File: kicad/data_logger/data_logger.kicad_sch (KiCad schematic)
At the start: 20 parts, among them M2 Motor_DC, M3 Motor_DC, M4 Motor_Servo, SW1 SW_SPST, SW2 SW_Reed

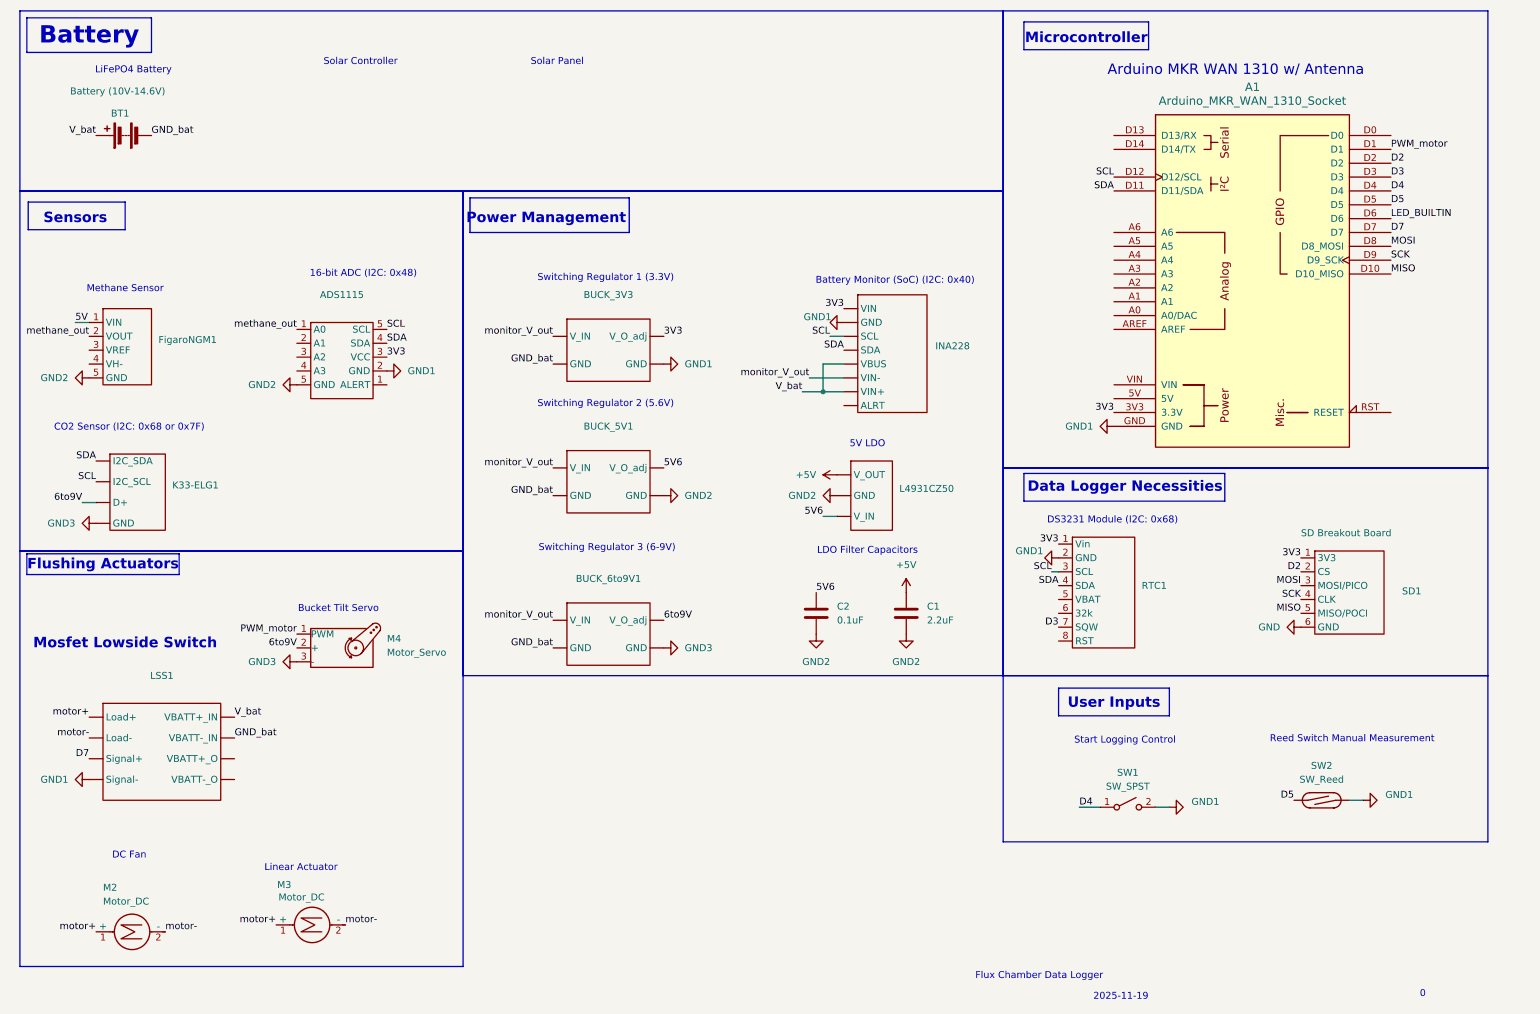
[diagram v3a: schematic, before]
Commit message: Schematic changes to add motor driver and routed traces
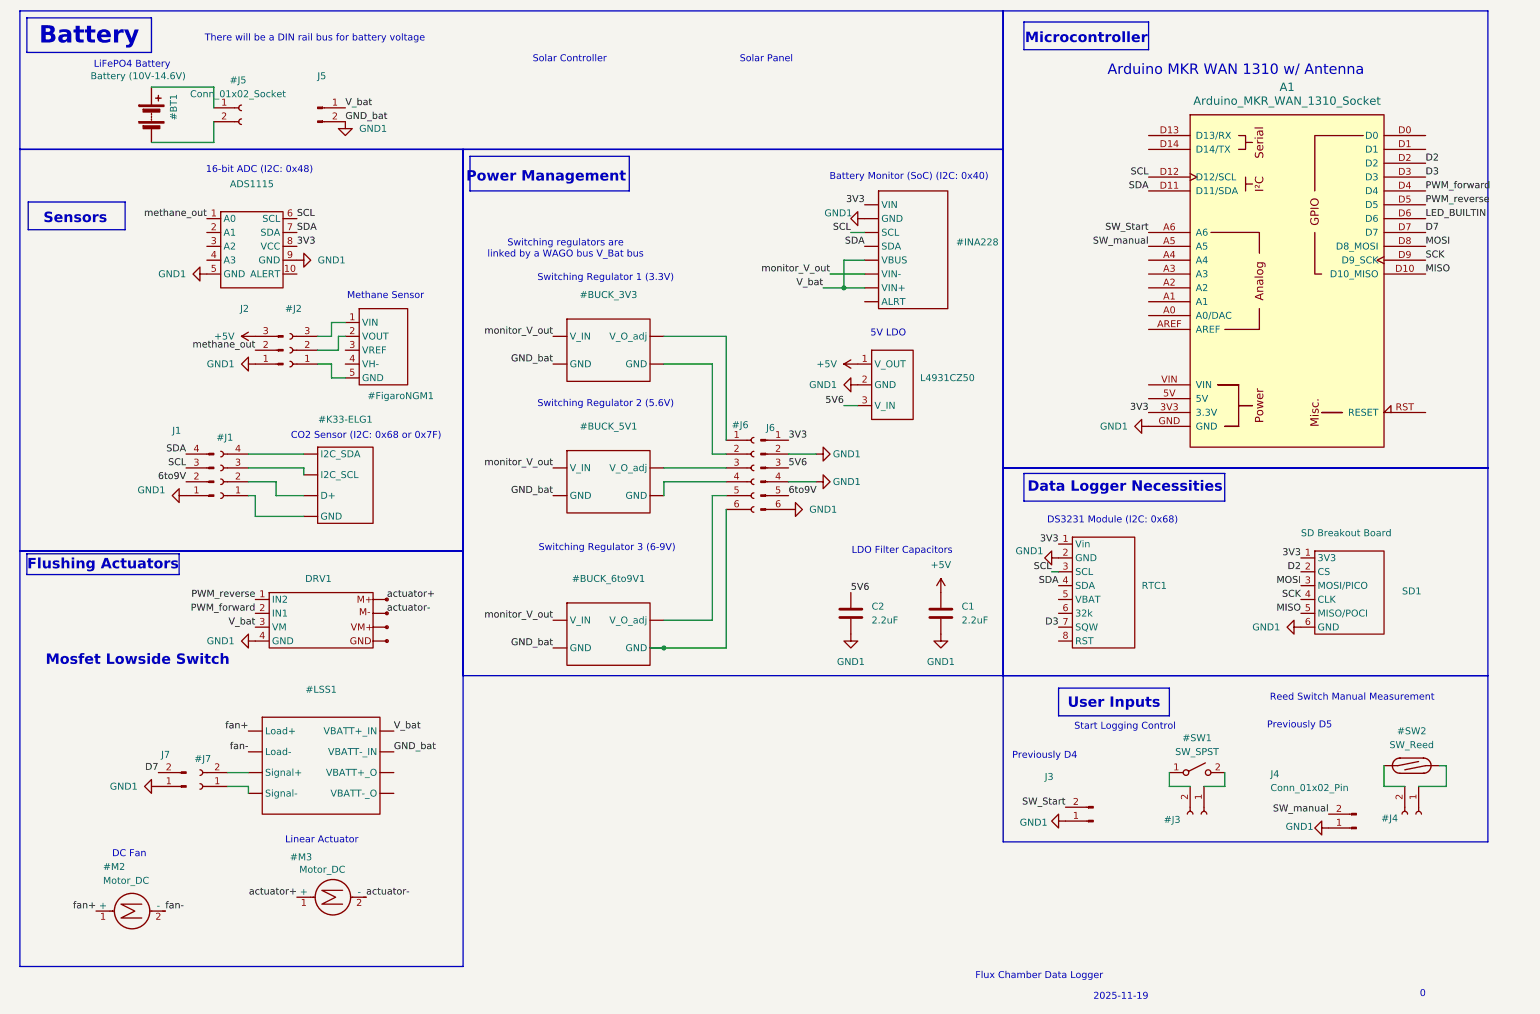
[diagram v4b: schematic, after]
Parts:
- removed M4: Motor_Servo, symbol Motor:Motor_Servo
- added #J1: Conn_01x04_Socket, Connector_JST:JST_XH_B4B-XH-A_1x04_P2.50mm_Vertical, symbol Connector:Conn_01x04_Socket
- added #J2: Conn_01x03_Socket, Connector_JST:JST_XH_B3B-XH-A_1x03_P2.50mm_Vertical, symbol Connector:Conn_01x03_Socket
- added #J3, #J4, #J5, #J7: Conn_01x02_Socket, symbol Connector:Conn_01x02_Socket
- added #J6: Conn_01x06_Socket, symbol Connector:Conn_01x06_Socket
- added DRV1: ~, new_library:DRV8871, symbol new_library:DRV8871
- added J1: Conn_01x04_Pin, Connector_JST:JST_XH_B4B-XH-A_1x04_P2.50mm_Vertical, symbol Connector:Conn_01x04_Pin
- added J2: Conn_01x03_Pin, Connector_JST:JST_XH_B3B-XH-A_1x03_P2.50mm_Vertical, symbol Connector:Conn_01x03_Pin
- added J3, J4, J5, J7: Conn_01x02_Pin, Connector_JST:JST_XH_B2B-XH-A_1x02_P2.50mm_Vertical, symbol Connector:Conn_01x02_Pin
- added J6: Conn_01x06_Pin, Connector_JST:JST_XH_B6B-XH-A_1x06_P2.50mm_Vertical, symbol Connector:Conn_01x06_Pin
- ADS1115: footprint new_library:ADC_16-bit_ADS1115_breakout -> new_library:ADS1115_breakout_soldered
- C1: footprint (none) -> Capacitor_THT:C_Disc_D5.0mm_W2.5mm_P5.00mm
- C2: value 0.1uF -> 2.2uF; footprint (none) -> Capacitor_THT:C_Disc_D5.0mm_W2.5mm_P5.00mm
- L4931CZ50: footprint (none) -> Package_TO_SOT_THT:TO-92L_Inline
- renumbered BT1 to #BT1, BUCK_3V3 to #BUCK_3V3, BUCK_5V1 to #BUCK_5V1, BUCK_6to9V1 to #BUCK_6to9V1, FigaroNGM1 to #FigaroNGM1, INA228 to #INA228, K33-ELG1 to #K33-ELG1, LSS1 to #LSS1, M2 to #M2, M3 to #M3, SW1 to #SW1, SW2 to #SW2
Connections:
- net GND is gone; now on net GND1: SD1.6 (GND)
- net +5V: now also L4931CZ50.1 (V_OUT), J2.3 (Pin_3); no longer L4931CZ50. (V_IN)
- net 3V3: now also ADS1115.8 (VCC), J6.1 (Pin_1); no longer #BUCK_3V3. (GND), ADS1115.3 (VCC)
- net 5V6: now also L4931CZ50.3 (V_IN), J6.3 (Pin_3); no longer #BUCK_5V1. (GND), L4931CZ50. (V_IN)
- net 6to9V: now also J1.2 (Pin_2), J6.5 (Pin_5); no longer #BUCK_6to9V1. (GND), #K33-ELG1. (GND)
- net D7: now also J7.2 (Pin_2); no longer #LSS1. (VBATT-_O)
- net GND1: now also #BUCK_5V1. (GND), #BUCK_6to9V1. (GND), ADS1115.5 (GND), ADS1115.9 (GND), C1.2, C2.2, L4931CZ50.2 (GND), DRV1.4 (GND), J1.1 (Pin_1), J2.1 (Pin_1), J3.1 (Pin_1), J4.1 (Pin_1), J5.2 (Pin_2), J6.2 (Pin_2), J6.4 (Pin_4), J6.6 (Pin_6), J7.1 (Pin_1); no longer #SW1.2 (B), #SW2.2, ADS1115.2 (GND)
- net SCL: now also ADS1115.6 (SCL), J1.3 (Pin_3); no longer #K33-ELG1. (GND), ADS1115.5 (SCL)
- net SDA: now also ADS1115.7 (SDA), J1.4 (Pin_4); no longer #K33-ELG1. (GND), ADS1115.4 (SDA)
- net V_bat: now also DRV1.3 (VM), J5.1 (Pin_1); no longer #BT1.1 (+)
- net methane_out: now also J2.2 (Pin_2); no longer #FigaroNGM1.2 (VOUT)
- net fan-: now reaches #LSS1. (VBATT-_O)
- net fan-: now also #M2.2 (-)
- net SW_manual: now reaches A1.A5
- net SW_manual: now also J4.2 (Pin_2)
- net SW_Start: now reaches A1.A6
- net SW_Start: now also J3.2 (Pin_2)
- net 5V: no longer names the net of #FigaroNGM1.1 (VIN)
- net 5V: now also #J2.3 (Pin_3)
- net D4: no longer names the net of #SW1.1 (A)
- net D4: now also #J3.2 (Pin_2); no longer A1.D4
- net D5: no longer names the net of #SW2.1
- net D5: now also #J4.2 (Pin_2); no longer A1.D5
- removed net GND2: #BUCK_5V1. (GND), #FigaroNGM1.5 (GND), ADS1115.5 (SCL), C1.2, C2.2, L4931CZ50. (V_IN)
- net GND3: no longer names the net of #K33-ELG1. (GND)
- net GND3: now also #J1.4 (Pin_4); no longer #BUCK_6to9V1. (GND)
- removed net GND_bat: #BT1.2 (-), #BUCK_3V3. (GND), #BUCK_5V1. (GND), #BUCK_6to9V1. (GND), #LSS1. (VBATT-_O)
- net PWM_motor: no longer names the net of A1.D1
- removed net motor+: #LSS1. (VBATT-_O), #M2.1 (+), #M3.1 (+)
- removed net motor-: #LSS1. (VBATT-_O), #M2.2 (-), #M3.2 (-)
- new net: #BT1.1 (+), #J5.1 (Pin_1)
- new net: #BT1.2 (-), #J5.2 (Pin_2)
- new net: #J3.1 (Pin_1), #SW1.2 (B)
- new net: #J4.1 (Pin_1), #SW2.2
- new net: #BUCK_5V1. (GND), #J6.3 (Pin_3)
- new net: #BUCK_5V1. (GND), #J6.4 (Pin_4)
- new net: #FigaroNGM1.5 (GND), #J2.1 (Pin_1)
- new net: #FigaroNGM1.2 (VOUT), #J2.2 (Pin_2)
- new net: #J1.1 (Pin_1), #K33-ELG1. (GND)
- new net: #J1.2 (Pin_2), #K33-ELG1. (GND)
- new net: #J1.3 (Pin_3), #K33-ELG1. (GND)
- new net: #J7.1 (Pin_1), #LSS1. (VBATT-_O)
- new net: #J7.2 (Pin_2), #LSS1. (VBATT-_O)
- new net: #BUCK_3V3. (GND), #J6.1 (Pin_1)
- new net: #BUCK_3V3. (GND), #J6.2 (Pin_2)
- new net: #BUCK_6to9V1. (GND), #J6.5 (Pin_5)
- new net: #BUCK_6to9V1. (GND), #J6.6 (Pin_6)
- new net PWM_forward: A1.D4, DRV1.2 (IN1)
- new net PWM_reverse: A1.D5, DRV1.1 (IN2)
- new net actuator+: #M3.1 (+)
- new net actuator-: #M3.2 (-)
- new net fan+: #LSS1. (VBATT-_O), #M2.1 (+)
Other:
- note added: "Previously D4"
- note added: "Previously D5"
- note added: "Switching regulators are linked by a WAGO bus V_Bat bus"
- note added: "There will be a DIN rail bus for battery voltage"
- note removed: "Bucket Tilt Servo"
- moved on the sheet: A1, ADS1115, C1, C2

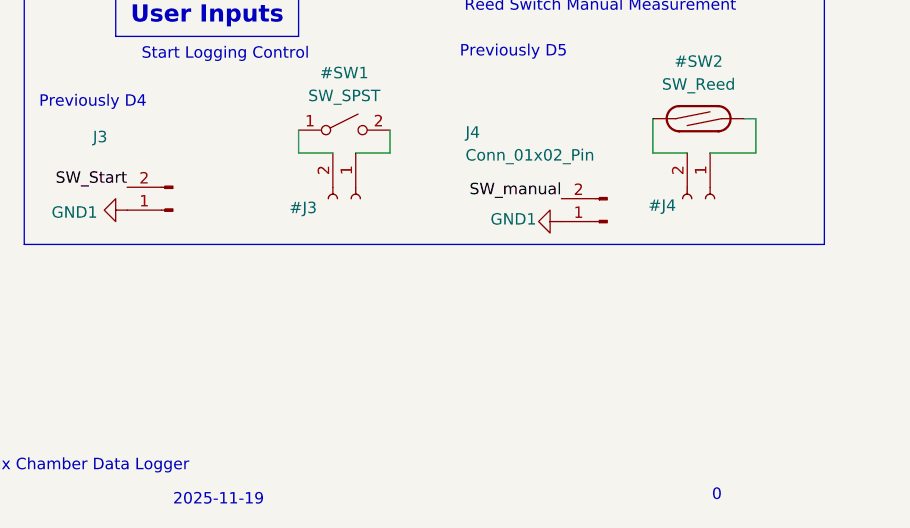
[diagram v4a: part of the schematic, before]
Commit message: Forgot to check if inputs were functional with external interrupts when I rearranged pins... Shouldve taken better notes!
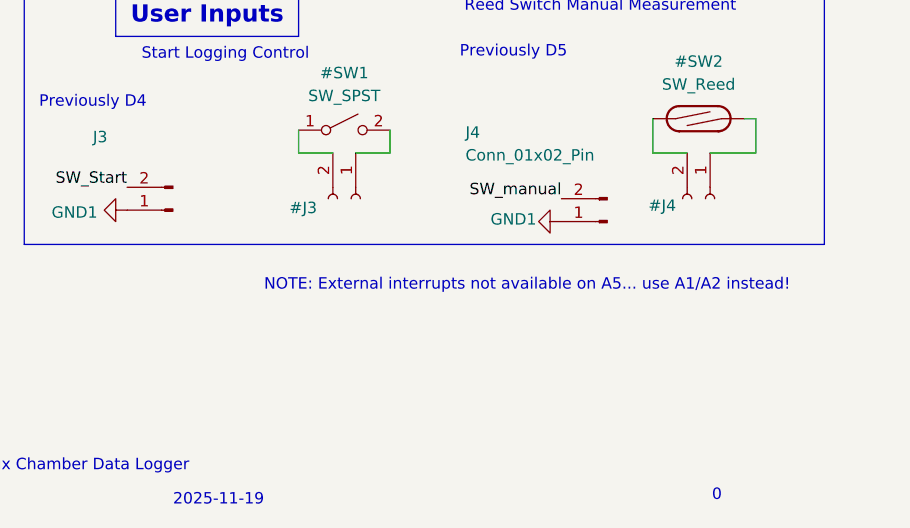
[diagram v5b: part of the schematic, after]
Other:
- note added: "NOTE: External interrupts not available on A5... use A1/A2 instead!"
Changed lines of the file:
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@@
+		)
+	)
+	(text "NOTE: External interrupts not available on A5... use A1/A2 instead!"
+		(exclude_from_sim no)
+		(at 248.92 169.672 0)
+		(effects
+			(font
+				(size 1.27 1.27)
+			)
 		)
 	)
